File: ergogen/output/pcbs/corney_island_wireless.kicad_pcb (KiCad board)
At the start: 2 copper layers, 133.8 x 91.7 mm, 94 parts

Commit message: Update assets
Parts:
- removed B1: Reset (PTS636 SP43 LFS), ceoloide:top-actuated-reset-switch
- removed LED1, LED10, LED11, LED12, LED13, LED14, LED15, LED16, LED17, LED18, LED19, LED2, LED20, LED21, LED3, LED4, LED5, LED6, LED7, LED8, LED9: , ceoloide:YS-SK6812MINI-E (per-key)
- removed LED22, LED23, LED24, LED25, LED26, LED27: , ceoloide:YS-SK6812MINI-E (underglow)
- removed TRRS1: TRRS-PJ-320A-dual, ceoloide:TRRS-PJ-320A-dual (reversible, symmetric)
- added SW1: , power_switch, F.Cu at (223.0, 99.2)
- added SW2: , sw_reset_side, F.Cu at (223.0, 91.2)
- added _1: , JST_PH_S2B-PH-K, F.Cu at (216.5, 96.5)
- moved DISP1 2.06 mm to (214.6, 93.3)
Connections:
- DISP1 pad 1: DISP1_1 -> GND
- DISP1 pad 2: DISP1_2 -> VCC
- DISP1 pad 3: DISP1_3 -> SCL
- DISP1 pad 4: DISP1_4 -> SDA
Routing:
- net VCC: track 101.4 -> 0.00 mm, vias 27 -> 0
- net GND: track 101.4 -> 0.00 mm, vias 27 -> 0
- net ULED_6: track 13.5 -> 0.00 mm, vias 2 -> 0
- net LED_1: track 13.5 -> 0.00 mm, vias 2 -> 0
- net ULED_5: track 13.5 -> 0.00 mm, vias 2 -> 0
- net ULED_4: track 13.5 -> 0.00 mm, vias 2 -> 0
- net ULED_3: track 13.5 -> 0.00 mm, vias 2 -> 0
- net ULED_2: track 13.5 -> 0.00 mm, vias 2 -> 0
- net ULED_1: track 13.5 -> 0.00 mm, vias 2 -> 0
- net LED_9: track 13.5 -> 0.00 mm, vias 2 -> 0
- net LED_6: track 13.5 -> 0.00 mm, vias 2 -> 0
- net LED_5: track 13.5 -> 0.00 mm, vias 2 -> 0
- net LED_4: track 13.5 -> 0.00 mm, vias 2 -> 0
- net LED_3: track 13.5 -> 0.00 mm, vias 2 -> 0
- net LED_20: track 13.5 -> 0.00 mm, vias 2 -> 0
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
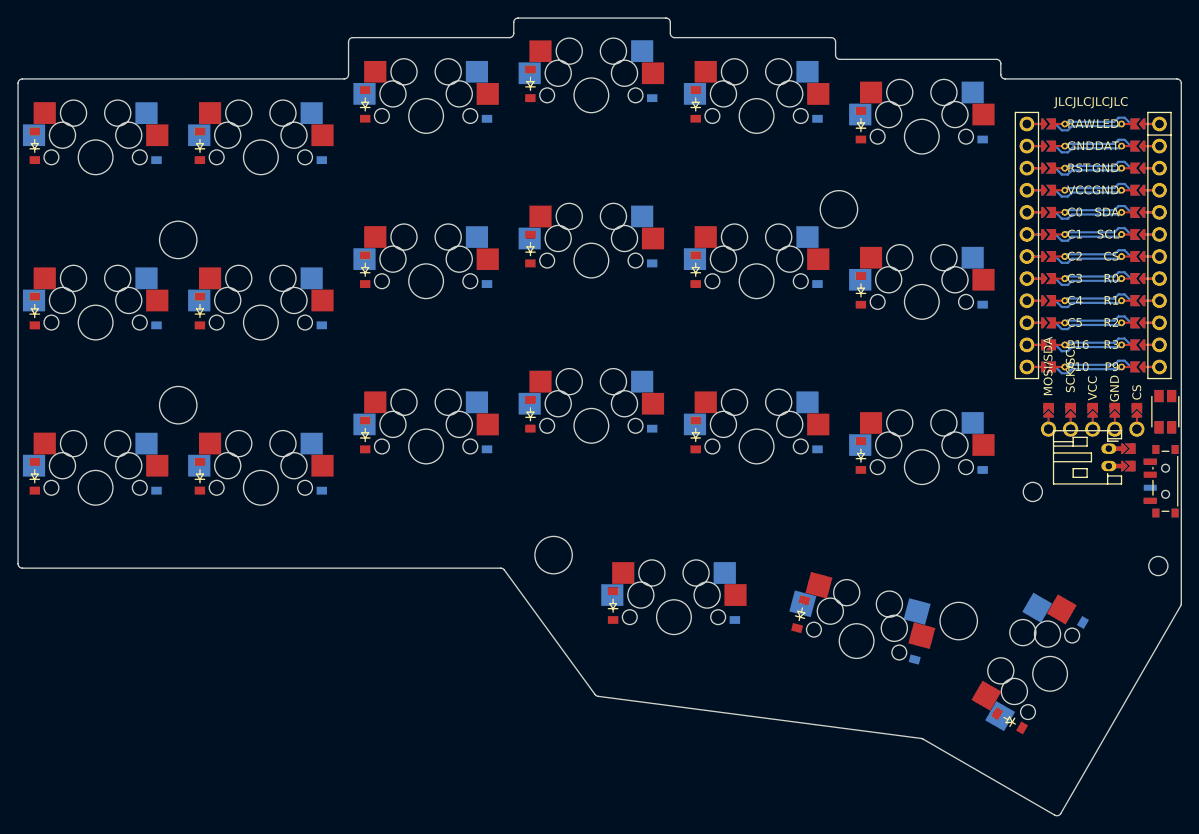
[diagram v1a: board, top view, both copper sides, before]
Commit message: Update wireless assets
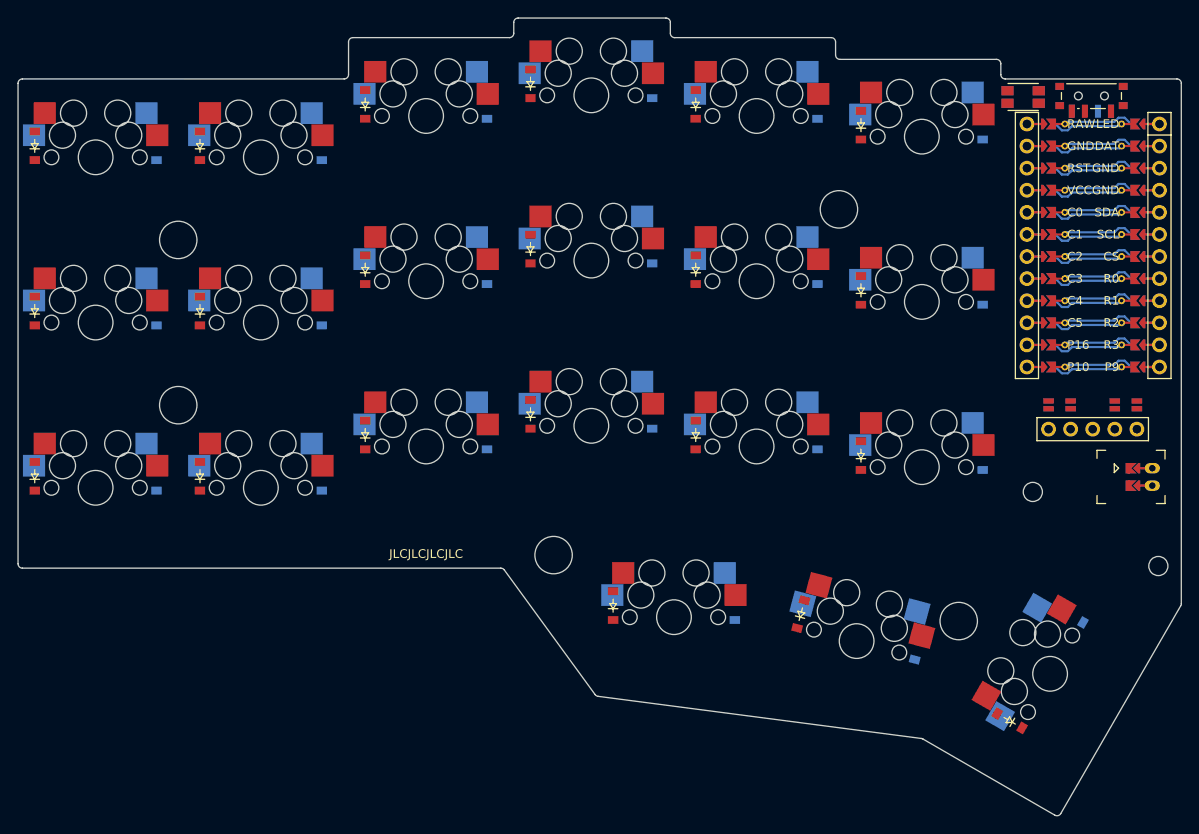
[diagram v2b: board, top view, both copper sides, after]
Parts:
- removed _1: , JST_PH_S2B-PH-K
- added JST1: , JST_PH_S2B-PH-K, F.Cu at (221.5, 98.8)
- DISP1: footprint combo_display -> nice!view
- moved SW1 45.1 mm to (214.5, 55.0), turned to 90 degrees
- moved SW2 39.7 mm to (206.7, 55.1), turned to 90 degrees
- moved DISP1 16.7 mm to (214.6, 76.6)
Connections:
- DISP1 pad 1: GND -> DISP1_1
- DISP1 pad 2: VCC -> DISP1_2
- DISP1 pad 3: SCL -> VCC
- DISP1 pad 4: SDA -> DISP1_4
- DISP1 pad 5: CS -> DISP1_5
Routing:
- net JST1_2: track 0.00 -> 3.60 mm
- net JST1_1: track 0.00 -> 3.60 mm

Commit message: Update assets
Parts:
- moved DISP1 3.30 mm to (214.6, 73.3)
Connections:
- DISP1 pad 10: DISP1_1 -> CS
- DISP1 pad 11: DISP1_2 -> GND
- DISP1 pad 12: DISP1_4 -> SCL
- DISP1 pad 13: DISP1_5 -> SDA
- DISP1 pad 14: SDA -> DISP1_1
- DISP1 pad 15: SCL -> DISP1_2
- DISP1 pad 16: GND -> DISP1_4
- DISP1 pad 17: CS -> DISP1_5
- DISP1 pad 20: DISP1_5 -> CS
- DISP1 pad 21: DISP1_4 -> GND
- DISP1 pad 22: DISP1_2 -> SCL
- DISP1 pad 23: DISP1_1 -> SDA
- DISP1 pad 24: SDA -> DISP1_5
- DISP1 pad 25: SCL -> DISP1_4
- DISP1 pad 26: GND -> DISP1_2
- DISP1 pad 27: CS -> DISP1_1

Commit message: Update assets
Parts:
- moved DISP1 0.49 mm to (214.6, 73.8)
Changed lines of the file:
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@@
       )
       (module nice!view (layer F.Cu)
-        (at 214.647 73.258 0)
+        (at 214.647 73.75 0)
         (attr virtual)
         (fp_text reference "DISP1" (at 0 20 0) (layer F.SilkS) hide

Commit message: Update assets
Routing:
- net SDA: track 0.00 -> 4.90 mm
- net SCL: track 0.00 -> 4.90 mm
- net GND: track 0.00 -> 4.90 mm
- net CS: track 0.00 -> 4.90 mm
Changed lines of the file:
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@@
       (fp_line (start -5.4 13.4) (end 5.4 13.4) (layer Dwgs.User) (width 0.15))
     )
+    (segment (start 209.567 90.450) (end 209.567 92.900) (width 0.15) (layer "F.Cu") (net 42))
+    (segment (start 212.107 90.450) (end 212.107 92.900) (width 0.25) (layer "F.Cu") (net 33))
+    (segment (start 217.187 90.450) (end 217.187 92.900) (width 0.15) (layer "F.Cu") (net 41))
+    (segment (start 219.727 90.450) (end 219.727 92.900) (width 0.15) (layer "F.Cu") (net 40))
+    (segment (start 209.567 90.450) (end 209.567 92.900) (width 0.15) (layer "B.Cu") (net 42))
+    (segment (start 212.107 90.450) (end 212.107 92.900) (width 0.15) (layer "B.Cu") (net 33))
+    (segment (start 217.187 90.450) (end 217.187 92.900) (width 0.25) (layer "B.Cu") (net 41))
+    (segment (start 219.727 90.450) (end 219.727 92.900) (width 0.15) (layer "B.Cu") (net 40))
         (module power_switch (layer F.Cu)
           (at 214.5 54.97 90)

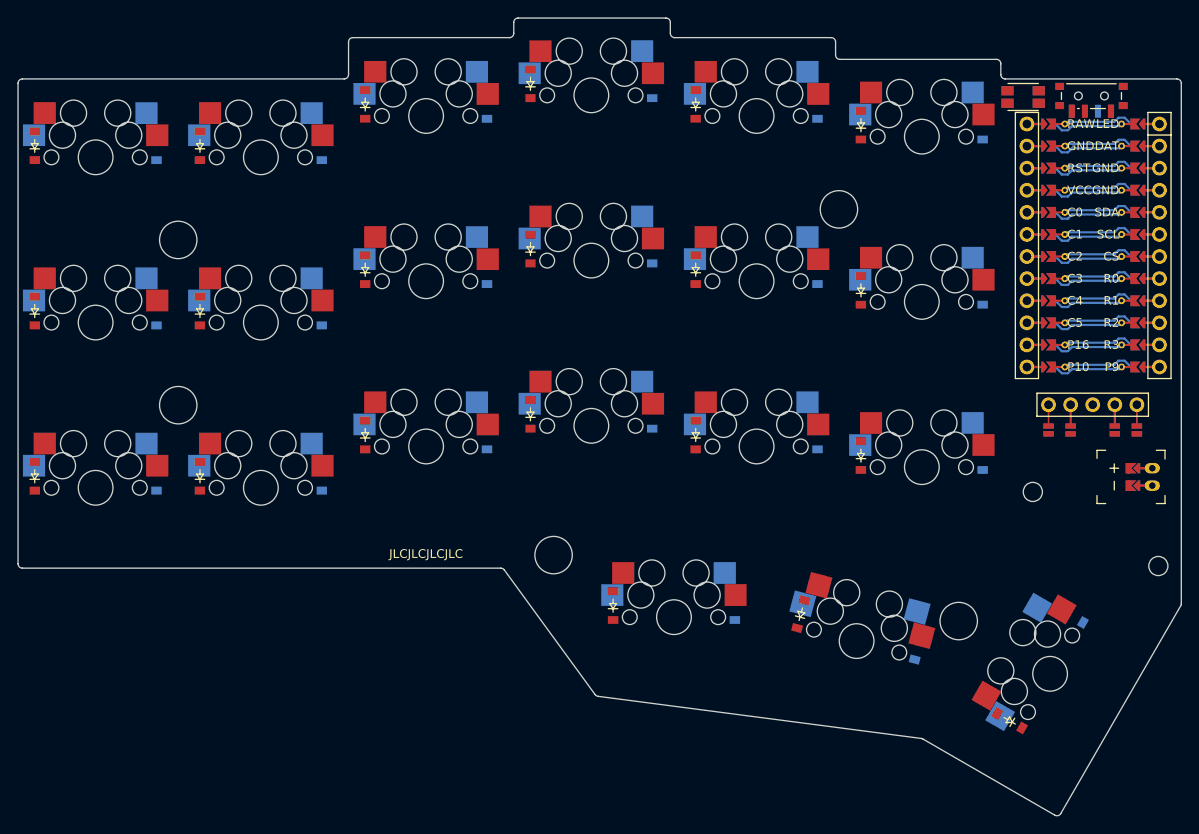
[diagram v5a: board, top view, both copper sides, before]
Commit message: Update TRRS footprint pinout and module
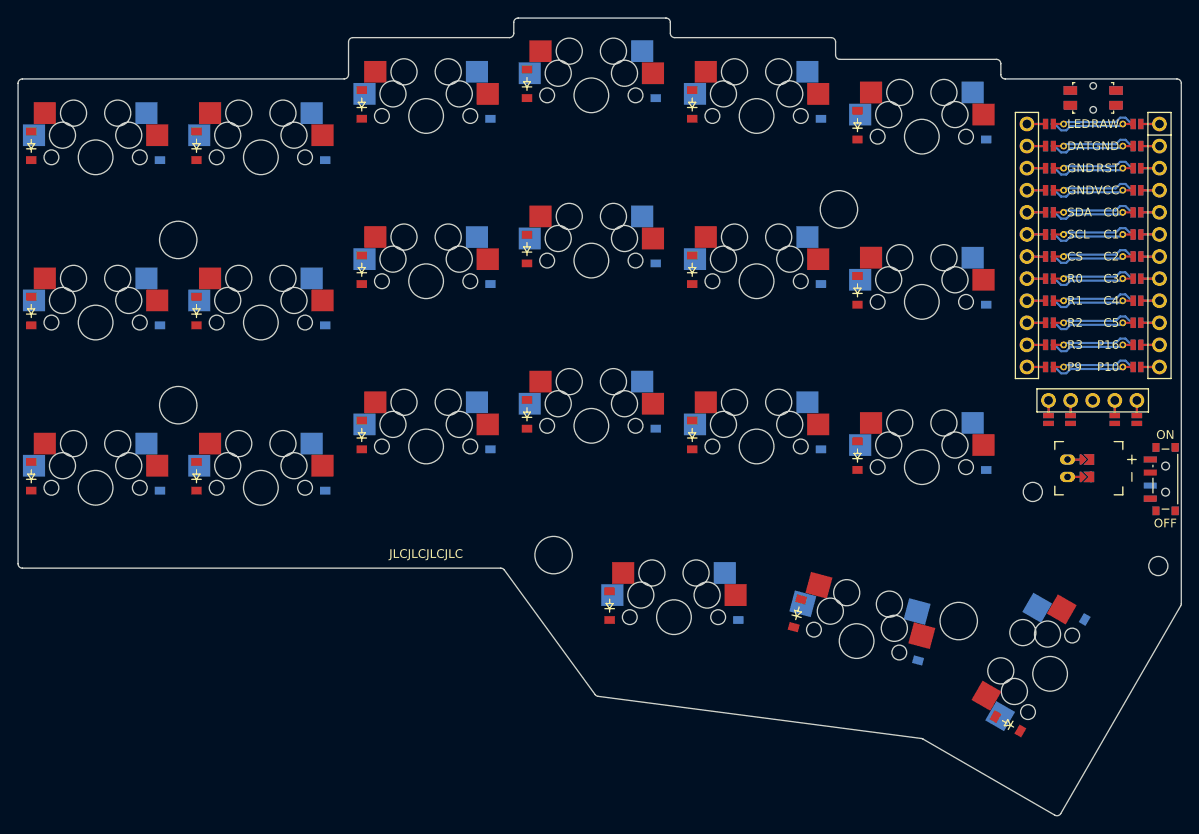
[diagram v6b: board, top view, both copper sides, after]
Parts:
- removed SW1: , power_switch
- removed SW2: , sw_reset_side
- added MH1: , ceoloide:mounting_hole_npth, F.Cu at (207.8, 100.5)
- added MH2: , ceoloide:mounting_hole_npth, F.Cu at (222.2, 109.0)
- added MH3: , ceoloide:mounting_hole_npth, F.Cu at (109.5, 71.5)
- added MH4: , ceoloide:mounting_hole_npth, F.Cu at (109.5, 90.5)
- added MH5: , ceoloide:mounting_hole_npth, F.Cu at (185.5, 68.0)
- added MH6: , ceoloide:mounting_hole_npth, F.Cu at (152.7, 107.7)
- added MH7: , ceoloide:mounting_hole_npth, F.Cu at (199.2, 115.3)
- added PWR1: power_switch, ceoloide:power_switch_smd_side, F.Cu at (223.0, 99.0)
- added RST1: reset_button_smd_side, ceoloide:reset_button_smd_side, F.Cu at (214.7, 55.2)
- D1, D10, D11, D12, D13, D14, D15, D16, D17, D18, D19, D2, D20, D21, D22, D23, D24, D25, D26, D27, D28, D29, D3, D30, D31, D32, D33, D34, D35, D36, D37, D38, D39, D4, D40, D41, D42, D5, D6, D7, D8, D9: footprint ComboDiode -> ceoloide:diode_tht_sod123
- DISP1: footprint nice!view -> ceoloide:nice_view
- JST1: footprint JST_PH_S2B-PH-K -> ceoloide/battery_connector_jst_ph_2
- MCU1: footprint nice_nano -> ceoloide:nice_nano
- moved JST1 9.80 mm to (211.8, 97.8), turned to 90 degrees
- moved DISP1 0.50 mm to (214.6, 73.2)
- moved D41 0.40 mm to (180.7, 114.4)
- moved D21 0.40 mm to (212.3, 114.3)
- moved D42 0.40 mm to (204.9, 127.1)
- moved D1 0.40 mm to (107.4, 98.7)
- moved D10 0.40 mm to (164.4, 91.5)
- moved D11 0.40 mm to (164.4, 72.5)
- moved D12 0.40 mm to (164.4, 53.5)
- moved D13 0.40 mm to (183.4, 93.9)
- moved D14 0.40 mm to (183.4, 74.9)
- moved D15 0.40 mm to (183.4, 55.9)
- moved D16 0.40 mm to (202.4, 96.3)
- moved D17 0.40 mm to (202.4, 77.3)
- moved D18 0.40 mm to (202.4, 58.3)
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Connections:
- JST1 pad 1: GND -> BAT_P
- JST1 pad 2: BAT_P -> GND
- MCU1 pad 1: MCU1_1 -> RAW
- MCU1 pad 10: MCU1_10 -> C5
- MCU1 pad 11: MCU1_11 -> P16
- MCU1 pad 12: MCU1_12 -> P10
- MCU1 pad 13: MCU1_13 -> MCU1_12
- MCU1 pad 14: MCU1_14 -> MCU1_11
- MCU1 pad 15: MCU1_15 -> MCU1_10
- MCU1 pad 16: MCU1_16 -> MCU1_9
- MCU1 pad 17: MCU1_17 -> MCU1_8
- MCU1 pad 18: MCU1_18 -> MCU1_7
- MCU1 pad 19: MCU1_19 -> MCU1_6
- MCU1 pad 2: MCU1_2 -> GND
- MCU1 pad 20: MCU1_20 -> MCU1_5
- MCU1 pad 21: MCU1_21 -> MCU1_4
- MCU1 pad 22: MCU1_22 -> MCU1_3
- MCU1 pad 23: MCU1_23 -> MCU1_2
- MCU1 pad 24: MCU1_24 -> MCU1_1
- MCU1 pad 3: MCU1_3 -> RST
- MCU1 pad 4: MCU1_4 -> VCC
- MCU1 pad 5: MCU1_5 -> C0
- MCU1 pad 6: MCU1_6 -> C1
- MCU1 pad 7: MCU1_7 -> C2
- MCU1 pad 8: MCU1_8 -> C3
- MCU1 pad 9: MCU1_9 -> C4
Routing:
- net C0: track 121.9 -> 14.2 mm
- net C3: track 121.8 -> 14.2 mm
- net index_top: track 0.00 -> 101.6 mm
- net outer_bottom: track 0.00 -> 101.4 mm
- net SDA: track 4.90 -> 3.50 mm
- net SCL: track 4.90 -> 3.50 mm
- net GND: track 4.90 -> 3.50 mm
- net CS: track 4.90 -> 3.50 mm
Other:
- outline, holes or cut-outs redrawn

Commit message: Update assets
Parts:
- DISP1: footprint ceoloide:nice_view -> ceoloide:display_nice_view
- JST1: footprint ceoloide/battery_connector_jst_ph_2 -> ceoloide:battery_connector_jst_ph_2
- MCU1: footprint ceoloide:nice_nano -> ceoloide:mcu_nice_nano
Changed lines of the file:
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@@
             (pad 2 smd rect (at 1.65 0 150) (size 0.9 1.2) (layers F.Cu F.Paste F.Mask) (net 27 "far_home"))
         )
-        (module "ceoloide:nice_nano" (layer F.Cu)
+        (module "ceoloide:mcu_nice_nano" (layer F.Cu)
           (attr virtual)
           (at 214.704 70.87 0)
@@
          (justify mirror))
       )
-      (module "ceoloide:nice_view" (layer F.Cu)
+      (module "ceoloide:display_nice_view" (layer F.Cu)
         (at 214.647 73.25 0)
         (attr virtual)
@@
         (fp_line (start 2.35 1.5) (end 2.35 1.75) (width 0.1) (layer "B.SilkS"))
       )
-            (module "ceoloide/battery_connector_jst_ph_2" (layer F.Cu)
+            (module "ceoloide:battery_connector_jst_ph_2" (layer F.Cu)
                 (at 211.75 97.75 90)
                 (descr "JST PH series connector, S2B-PH-K (http://www.jst-mfg.com/product/pdf/eng/ePH.pdf)")
